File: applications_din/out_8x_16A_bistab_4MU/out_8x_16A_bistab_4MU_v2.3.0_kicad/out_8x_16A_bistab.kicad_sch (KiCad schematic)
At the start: 30 parts, among them IC1 ULN2803A, IC2 ULN2803A, J1 Screw_Terminal_01x02, K1 HFE20-1-024-1HD504, K2 HFE20-1-024-1HD504, K3 HFE20-1-024-1HD504, K4 HFE20-1-024-1HD504, K5 HFE20-1-024-1HD504, K6 HFE20-1-024-1HD504, K7 HFE20-1-024-1HD504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

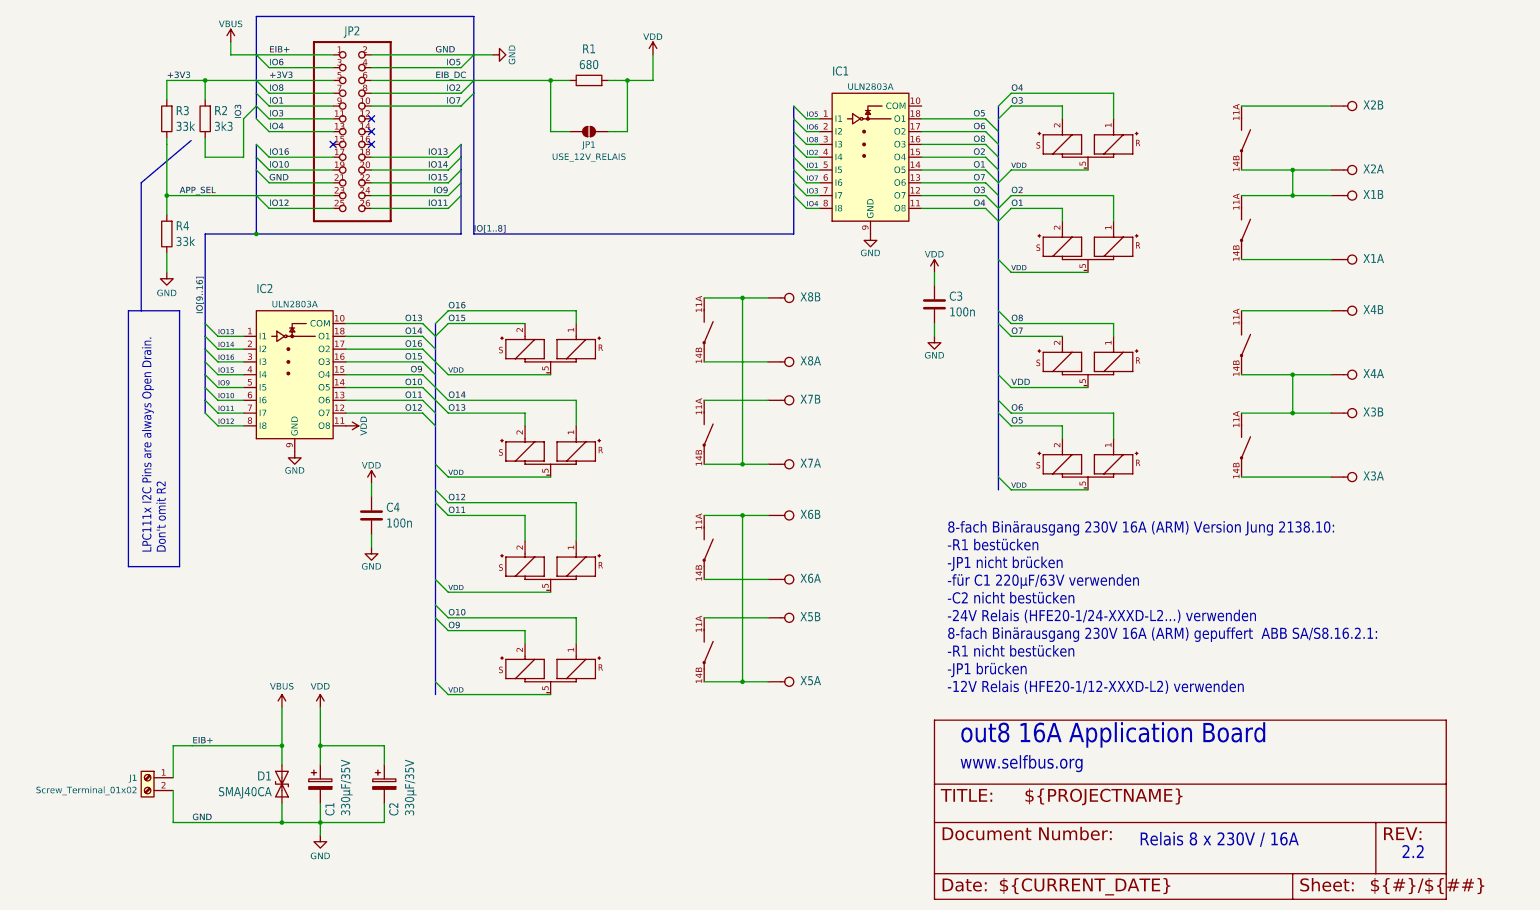
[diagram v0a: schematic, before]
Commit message: out 8x 16A bistab 4MU is now v2.3.0 kicad
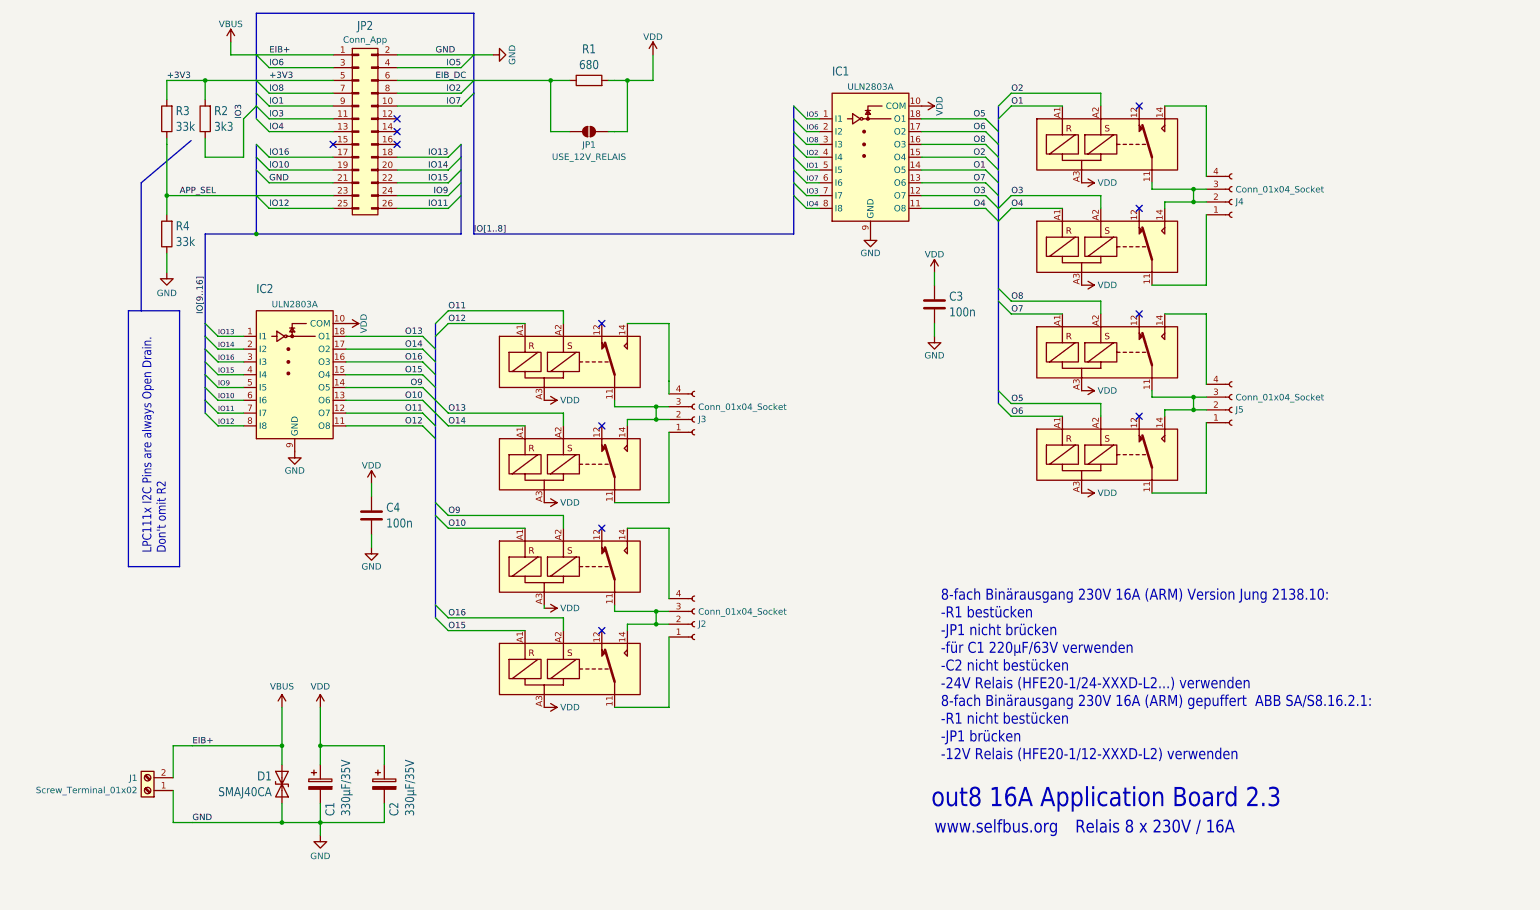
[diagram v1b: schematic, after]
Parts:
- removed unit 2 of K1
- removed unit 2 of K2
- removed unit 2 of K3
- removed unit 2 of K4
- removed unit 2 of K5
- removed unit 2 of K6
- removed unit 2 of K7
- removed unit 2 of K8
- removed X1, X2, X3, X4, X5, X6, X7, X8: W237-02P, out_8x_16A_bistab:W237-132, symbol out_8x_16A_bistab-eagle-import:W237-02P
- added J2, J3, J4, J5: Conn_01x04_Socket, TerminalBlock_Altech:Altech_AK100_1x04_P5.00mm, symbol Connector:Conn_01x04_Socket
- C1, C2: footprint out_8x_16A_bistab:E3,5-8 -> Capacitor_THT:CP_Radial_D8.0mm_P3.50mm
- C3, C4: footprint out_8x_16A_bistab:C1206 -> Capacitor_SMD:C_0805_2012Metric
- IC1, IC2: footprint out_8x_16A_bistab:SO18W -> Package_SO:SOIC-18W_7.5x11.6mm_P1.27mm
- J1: footprint (none) -> selfbus:W243-211_1x02_P5.75
- JP2: value A -> Conn_App; footprint out_8x_16A_bistab:2X13SMD -> Connector_PinHeader_2.54mm:PinHeader_2x13_P2.54mm_Vertical_SMD; symbol out_8x_16A_bistab-eagle-import:PINHD-2X13_2.54-SMD -> Connector_Generic:Conn_02x13_Odd_Even
- K1, K2, K3, K4, K5, K6, K7, K8: footprint out_8x_16A_bistab:HFE20-3-504 -> selfbus:HFE20-1-L2; symbol out_8x_16A_bistab-eagle-import:HFE20-1-024-1HD504 -> selfbus:HFE20-1/24-1HSD-L2
- R1, R2, R3, R4: footprint out_8x_16A_bistab:M1206 -> Resistor_SMD:R_0805_2012Metric
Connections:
- net GND: now also J1.1 (Pin_1); no longer J1.2 (Pin_2)
- net O1: now also K1.A1; no longer K1.2 (S+)
- net O10: now also IC2.13 (O6), K6.A1; no longer IC2.14 (O5), K5.1 (R+)
- net O11: now also IC2.12 (O7), K8.A2; no longer IC2.13 (O6), K6.2 (S+)
- net O12: now also IC2.11 (O8), K8.A1; no longer IC2.12 (O7), K6.1 (R+)
- net O13: now also IC2.18 (O1), K7.A2; no longer IC2.10 (COM), K7.2 (S+)
- net O14: now also IC2.17 (O2), K7.A1; no longer IC2.18 (O1), K7.1 (R+)
- net O15: now also IC2.15 (O4), K5.A1; no longer IC2.16 (O3), K8.2 (S+)
- net O16: now also IC2.16 (O3), K5.A2; no longer IC2.17 (O2), K8.1 (R+)
- net O2: now also K1.A2; no longer K1.1 (R+)
- net O3: now also K2.A2; no longer K2.2 (S+)
- net O4: now also K2.A1; no longer K2.1 (R+)
- net O5: now also K4.A2; no longer K3.2 (S+)
- net O6: now also K4.A1; no longer K3.1 (R+)
- net O7: now also K3.A1; no longer K4.2 (S+)
- net O8: now also K3.A2; no longer K4.1 (R+)
- net O9: now also IC2.14 (O5), K6.A2; no longer IC2.15 (O4), K5.2 (S+)
- net VBUS: now also J1.2 (Pin_2); no longer J1.1 (Pin_1)
- net VDD: now also IC1.10 (COM), IC2.10 (COM), K1.A3, K2.A3, K3.A3, K4.A3, K5.A3, K6.A3, K7.A3, K8.A3; no longer IC2.11 (O8), K1.5 (-), K2.5 (-), K3.5 (-), K4.5 (-), K5.5 (-), K6.5 (-), K7.5 (-), K8.5 (-)
- new net: J2.1 (Pin_1), K5.11
- new net: J2.2 (Pin_2), J2.3 (Pin_3), K5.14, K6.11
- new net: J2.4 (Pin_4), K6.14
- new net: J3.1 (Pin_1), K7.11
- new net: J3.2 (Pin_2), J3.3 (Pin_3), K7.14, K8.11
- new net: J3.4 (Pin_4), K8.14
- new net: J5.2 (Pin_2), J5.3 (Pin_3), K3.11, K4.14
- new net: J5.4 (Pin_4), K3.14
- new net: J4.2 (Pin_2), J4.3 (Pin_3), K1.11, K2.14
- new net: J4.4 (Pin_4), K1.14
- new net: J4.1 (Pin_1), K2.11
- new net: J5.1 (Pin_1), K4.11
- no-connect marks 4 -> 12
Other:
- note added: "out8 16A Application Board 2.3"
- note removed: "2.2"
- note removed: "out8 16A Application Board"
- moved on the sheet: J1

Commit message: update out_8x_16A_bistab_4MU_v2.3.0_kicad - final for now
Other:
- moved on the sheet: JP1, R1
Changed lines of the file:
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@@
 	)
 	(junction
-		(at 119.38 35.56)
+		(at 113.03 35.56)
 		(diameter 0)
 		(color 0 0 0 0)
@@
 	)
 	(junction
-		(at 104.14 35.56)
+		(at 97.79 35.56)
 		(diameter 0)
 		(color 0 0 0 0)
@@
 	(wire
 		(pts
-			(xy 115.57 35.56) (xy 116.84 35.56)
+			(xy 109.22 35.56) (xy 110.49 35.56)
 		)
 		(stroke
@@
 	(wire
 		(pts
-			(xy 116.84 35.56) (xy 119.38 35.56)
+			(xy 110.49 35.56) (xy 113.03 35.56)
 		)
 		(stroke
@@
 	(wire
 		(pts
-			(xy 119.38 35.56) (xy 124.46 35.56)
+			(xy 113.03 35.56) (xy 118.11 35.56)
 		)
 		(stroke
@@
 	(wire
 		(pts
-			(xy 124.46 35.56) (xy 124.46 30.48)
+			(xy 118.11 35.56) (xy 118.11 30.48)
 		)
 		(stroke
@@
 	(wire
 		(pts
-			(xy 119.38 45.72) (xy 116.84 45.72)
+			(xy 113.03 45.72) (xy 110.49 45.72)
 		)
 		(stroke
@@
 	(wire
 		(pts
-			(xy 115.57 45.72) (xy 116.84 45.72)
+			(xy 109.22 45.72) (xy 110.49 45.72)
 		)
 		(stroke
@@
 	(wire
 		(pts
-			(xy 88.9 35.56) (xy 104.14 35.56)
+			(xy 88.9 35.56) (xy 97.79 35.56)
 		)
 		(stroke
@@
 	(wire
 		(pts
-			(xy 104.14 45.72) (xy 107.95 45.72)
+			(xy 97.79 45.72) (xy 101.6 45.72)
 		)
 		(stroke
@@
 	(wire
 		(pts
-			(xy 104.14 35.56) (xy 107.95 35.56)
+			(xy 97.79 35.56) (xy 101.6 35.56)
 		)
 		(stroke
@@
 	(wire
 		(pts
-			(xy 104.14 35.56) (xy 104.14 45.72)
+			(xy 97.79 35.56) (xy 97.79 45.72)
 		)
 		(stroke
@@
 	(wire
 		(pts
-			(xy 119.38 35.56) (xy 119.38 45.72)
+			(xy 113.03 35.56) (xy 113.03 45.72)
 		)
 		(stroke
@@
 	(symbol
 		(lib_id "Device:R")
-		(at 111.76 35.56 90)
+		(at 105.41 35.56 90)
 		(unit 1)
 		(exclude_from_sim no)
@@
 		(fields_autoplaced yes)
 		(property "Reference" "R1"
-			(at 111.76 29.3494 90)
+			(at 105.41 29.3494 90)
 			(effects
 				(font
@@
 		)
 		(property "Value" "680"
-			(at 111.76 32.4738 90)
+			(at 105.41 32.4738 90)
 			(effects
 				(font
@@
 		)
 		(property "Footprint" "Resistor_SMD:R_0805_2012Metric"
-			(at 111.76 37.338 90)
+			(at 105.41 37.338 90)
 			(effects
 				(font
@@
 		)
 		(property "Datasheet" "~"
-			(at 111.76 35.56 0)
+			(at 105.41 35.56 0)
 			(effects
 				(font
@@
 		)
 		(property "Description" "Resistor"
-			(at 111.76 35.56 0)
+			(at 105.41 35.56 0)
 			(effects
 				(font
@@
 	(symbol
 		(lib_id "power:VDD")
-		(at 124.46 30.48 0)
+		(at 118.11 30.48 0)
 		(unit 1)
 		(exclude_from_sim no)
@@
 		(dnp no)
 		(property "Reference" "#PWR0104"
-			(at 124.46 34.29 0)
+			(at 118.11 34.29 0)
 			(effects
 				(font
@@
 		)
 		(property "Value" "VDD"
-			(at 124.46 26.924 0)
+			(at 118.11 26.924 0)
 			(effects
 				(font
@@
 		)
 		(property "Footprint" ""
-			(at 124.46 30.48 0)
+			(at 118.11 30.48 0)
 			(effects
 				(font
@@
 		)
 		(property "Datasheet" ""
-			(at 124.46 30.48 0)
+			(at 118.11 30.48 0)
 			(effects
 				(font
@@
 		)
 		(property "Description" "Power symbol creates a global label with name \"VDD\""
-			(at 124.46 30.48 0)
+			(at 118.11 30.48 0)
 			(effects
 				(font
@@
 	(symbol
 		(lib_id "Jumper:SolderJumper_2_Open")
-		(at 111.76 45.72 0)
+		(at 105.41 45.72 0)
 		(unit 1)
 		(exclude_from_sim yes)
@@
 		(fields_autoplaced yes)
 		(property "Reference" "JP1"
-			(at 111.76 48.3291 0)
+			(at 105.41 48.3291 0)
 			(effects
 				(font
@@
 		)
 		(property "Value" "USE_12V_RELAIS"
-			(at 111.76 50.7534 0)
+			(at 105.41 50.7534 0)
 			(effects
 				(font
@@
 		)
 		(property "Footprint" "Jumper:SolderJumper-2_P1.3mm_Open_Pad1.0x1.5mm"
-			(at 111.76 45.72 0)
+			(at 105.41 45.72 0)
 			(effects
 				(font
@@
 		)
 		(property "Datasheet" "~"
-			(at 111.76 45.72 0)
+			(at 105.41 45.72 0)
 			(effects
 				(font
@@
 		)
 		(property "Description" "Solder Jumper, 2-pole, open"
-			(at 111.76 45.72 0)
+			(at 105.41 45.72 0)
 			(effects
 				(font

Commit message: update all stuff
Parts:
- J1: value Screw_Terminal_01x02 -> EIB_WAGO_243-211
- J6: renamed from JP2; footprint Connector_PinHeader_2.54mm:PinHeader_2x13_P2.54mm_Vertical_SMD -> Connector_IDC:IDC-Header_2x13_P2.54mm_Vertical_SMD
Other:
- moved on the sheet: J2, J3, J4, J5

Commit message: finally standardize selected parts on all boards
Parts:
- added D2: 12V, Diode_SMD:D_MiniMELF, symbol Device:D_Zener
- J2, J3, J4, J5: value Conn_01x04_Socket -> Con_230V
- R1: footprint Resistor_SMD:R_0805_2012Metric -> Resistor_SMD:R_1206_3216Metric
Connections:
- net GND: now also D2.2 (A)
- net VDD: now also D2.1 (K)
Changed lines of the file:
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@@
 	(wire
 		(pts
+			(xy 118.11 44.45) (xy 118.11 45.72)
+		)
+		(stroke
+			(width 0)
+			(type default)
+		)
+	)
+	(wire
+		(pts
 			(xy 97.79 35.56) (xy 97.79 45.72)
 		)
@@
 	(wire
 		(pts
+			(xy 118.11 35.56) (xy 118.11 36.83)
+		)
+		(stroke
+			(width 0)
+			(type default)
+		)
+	)
+	(wire
+		(pts
 			(xy 226.06 101.6) (xy 226.06 102.87)
 		)
@@
 		(on_board yes)
 		(dnp no)
+		(fields_autoplaced yes)
 		(property "Reference" "J2"
-			(at 134.0612 143.4522 0)
+			(at 132.715 133.8283 0)
 			(effects
 				(font
 					(size 1.27 1.27)
 				)
-				(justify left)
 			)
 		)
-		(property "Value" "Conn_01x04_Socket"
-			(at 134.0612 141.0279 0)
+		(property "Value" "Con_230V"
+			(at 132.715 136.2526 0)
 			(effects
 				(font
 					(size 1.27 1.27)
 				)
-				(justify left)
 			)
 		)
@@
 			)
 		)
-		(property "Footprint" "Resistor_SMD:R_0805_2012Metric"
+		(property "Footprint" "Resistor_SMD:R_1206_3216Metric"
 			(at 105.41 37.338 90)
 			(effects
@@
 	)
 	(symbol
+		(lib_id "Device:D_Zener")
+		(at 118.11 40.64 270)
+		(unit 1)
+		(exclude_from_sim no)
+		(in_bom yes)
+		(on_board yes)
+		(dnp no)
+		(fields_autoplaced yes)
+		(property "Reference" "D2"
+			(at 120.142 39.4278 90)
+			(effects
+				(font
+					(size 1.27 1.27)
+				)
+				(justify left)
+			)
+		)
+		(property "Value" "12V"
+			(at 120.142 41.8521 90)
+			(effects
+				(font
+					(size 1.27 1.27)
+				)
+				(justify left)
+			)
+		)
+		(property "Footprint" "Diode_SMD:D_MiniMELF"
+			(at 118.11 40.64 0)
+			(effects
+				(font
+					(size 1.27 1.27)
+				)
+				(hide yes)
+			)
+		)
+		(property "Datasheet" "~"
+			(at 118.11 40.64 0)
+			(effects
+				(font
+					(size 1.27 1.27)
+				)
+				(hide yes)
+			)
+		)
+		(property "Description" "Zener diode"
+			(at 118.11 40.64 0)
+			(effects
+				(font
+					(size 1.27 1.27)
+				)
+				(hide yes)
+			)
+		)
+		(pin "2"
+		)
+		(pin "1"
+		)
+		(instances
+			(project ""
+				(path "/e17a8f7c-290a-48c4-8119-0faa75a2ce74"
+					(reference "D2")
+					(unit 1)
+				)
+			)
+		)
+	)
+	(symbol
 		(lib_id "Transistor_Array:ULN2803A")
 		(at 167.64 48.26 0)
@@
 	)
 	(symbol
+		(lib_id "power:GND")
+		(at 118.11 45.72 0)
+		(unit 1)
+		(exclude_from_sim no)
+		(in_bom yes)
+		(on_board yes)
+		(dnp no)
+		(property "Reference" "#PWR018"
+			(at 118.11 52.07 0)
+			(effects
+				(font
+					(size 1.27 1.27)
+				)
+				(hide yes)
+			)
+		)
+		(property "Value" "GND"
+			(at 118.11 49.53 0)
+			(effects
+				(font
+					(size 1.27 1.27)
+				)
+			)
+		)
+		(property "Footprint" ""
+			(at 118.11 45.72 0)
+			(effects
+				(font
+					(size 1.27 1.27)
+				)
+				(hide yes)
+			)
+		)
+		(property "Datasheet" ""
+			(at 118.11 45.72 0)
+			(effects
+				(font
+					(size 1.27 1.27)
+				)
+				(hide yes)
+			)
+		)
+		(property "Description" "Power symbol creates a global label with name \"GND\" , ground"
+			(at 118.11 45.72 0)
+			(effects
+				(font
+					(size 1.27 1.27)
+				)
+				(hide yes)
+			)
+		)
+		(pin "1"
+		)
+		(instances
+			(project "out_8x_16A_bistab"
+				(path "/e17a8f7c-290a-48c4-8119-0faa75a2ce74"
+					(reference "#PWR018")
+					(unit 1)
+				)
+			)
+		)
+	)
+	(symbol
 		(lib_id "power:PWR_FLAG")
 		(at 39.37 167.64 0)
@@
 		(on_board yes)
 		(dnp no)
+		(fields_autoplaced yes)
 		(property "Reference" "J4"
-			(at 240.7412 59.6322 0)
+			(at 239.395 50.0083 0)
 			(effects
 				(font
 					(size 1.27 1.27)
 				)
-				(justify left)
 			)
 		)
-		(property "Value" "Conn_01x04_Socket"
-			(at 240.7412 57.2079 0)
+		(property "Value" "Con_230V"
+			(at 239.395 52.4326 0)
 			(effects
 				(font
 					(size 1.27 1.27)
 				)
-				(justify left)
 			)
 		)
@@
 		(on_board yes)
 		(dnp no)
+		(fields_autoplaced yes)
 		(property "Reference" "J5"
-			(at 240.7412 101.5422 0)
+			(at 239.395 91.9183 0)
 			(effects
 				(font
 					(size 1.27 1.27)
 				)
-				(justify left)
 			)
 		)
-		(property "Value" "Conn_01x04_Socket"
-			(at 240.7412 99.1179 0)
+		(property "Value" "Con_230V"
+			(at 239.395 94.3426 0)
 			(effects
 				(font
 					(size 1.27 1.27)
 				)
-				(justify left)
 			)
 		)
@@
 		(on_board yes)
 		(dnp no)
+		(fields_autoplaced yes)
 		(property "Reference" "J3"
-			(at 134.0612 102.8122 0)
+			(at 132.715 93.1883 0)
 			(effects
 				(font
 					(size 1.27 1.27)
 				)
-				(justify left)
 			)
 		)
-		(property "Value" "Conn_01x04_Socket"
-			(at 134.0612 100.3879 0)
+		(property "Value" "Con_230V"
+			(at 132.715 95.6126 0)
 			(effects
 				(font
 					(size 1.27 1.27)
 				)
-				(justify left)
 			)
 		)

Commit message: final for manufacturing
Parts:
- J1: value EIB_WAGO_243-211 -> WAGO-243-211
- K1, K2, K3, K4, K5, K6, K7, K8: value HFE20-1-024-1HD504 -> HFE20-1/24-1HSD-L2
- R1: value 680 -> 680 500mW
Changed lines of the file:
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@@
 			)
 		)
-		(property "Value" "680"
+		(property "Value" "680 500mW"
 			(at 105.41 32.4738 90)
 			(effects
@@
 		(on_board yes)
 		(dnp no)
+		(fields_autoplaced yes)
 		(property "Reference" "K7"
-			(at 111.76 111.125 0)
+			(at 122.682 110.1978 0)
 			(effects
 				(font
 					(size 1.778 1.5113)
 				)
-				(justify left bottom)
-				(hide yes)
+				(justify left)
 			)
 		)
-		(property "Value" "HFE20-1-024-1HD504"
-			(at 110.49 108.204 0)
+		(property "Value" "HFE20-1/24-1HSD-L2"
+			(at 122.682 113.3222 0)
 			(effects
 				(font
 					(size 1.778 1.5113)
 				)
-				(justify left bottom)
-				(hide yes)
+				(justify left)
 			)
 		)
@@
 		(on_board yes)
 		(dnp no)
+		(fields_autoplaced yes)
 		(property "Reference" "K8"
-			(at 111.76 90.805 0)
+			(at 122.682 89.8778 0)
 			(effects
 				(font
 					(size 1.778 1.5113)
 				)
-				(justify left bottom)
-				(hide yes)
+				(justify left)
 			)
 		)
-		(property "Value" "HFE20-1-024-1HD504"
-			(at 110.49 87.884 0)
+		(property "Value" "HFE20-1/24-1HSD-L2"
+			(at 122.682 93.0022 0)
 			(effects
 				(font
 					(size 1.778 1.5113)
 				)
-				(justify left bottom)
-				(hide yes)
+				(justify left)
 			)
 		)
@@
 		(on_board yes)
 		(dnp no)
+		(fields_autoplaced yes)
 		(property "Reference" "K6"
-			(at 111.76 131.445 0)
+			(at 122.682 130.5178 0)
 			(effects
 				(font
 					(size 1.778 1.5113)
 				)
-				(justify left bottom)
-				(hide yes)
+				(justify left)
 			)
 		)
-		(property "Value" "HFE20-1-024-1HD504"
-			(at 110.49 128.524 0)
+		(property "Value" "HFE20-1/24-1HSD-L2"
+			(at 122.682 133.6422 0)
 			(effects
 				(font
 					(size 1.778 1.5113)
 				)
-				(justify left bottom)
-				(hide yes)
+				(justify left)
 			)
 		)
@@
 		(on_board yes)
 		(dnp no)
+		(fields_autoplaced yes)
 		(property "Reference" "K3"
-			(at 218.44 89.535 0)
+			(at 229.362 88.6078 0)
 			(effects
 				(font
 					(size 1.778 1.5113)
 				)
-				(justify left bottom)
-				(hide yes)
+				(justify left)
 			)
 		)
-		(property "Value" "HFE20-1-024-1HD504"
-			(at 217.17 86.614 0)
+		(property "Value" "HFE20-1/24-1HSD-L2"
+			(at 229.362 91.7322 0)
 			(effects
 				(font
 					(size 1.778 1.5113)
 				)
-				(justify left bottom)
-				(hide yes)
+				(justify left)
 			)
 		)
@@
 		(on_board yes)
 		(dnp no)
+		(fields_autoplaced yes)
 		(property "Reference" "K1"
-			(at 218.44 47.625 0)
+			(at 229.362 46.6978 0)
 			(effects
 				(font
 					(size 1.778 1.5113)
 				)
-				(justify left bottom)
-				(hide yes)
+				(justify left)
 			)
 		)
-		(property "Value" "HFE20-1-024-1HD504"
-			(at 217.17 44.704 0)
+		(property "Value" "HFE20-1/24-1HSD-L2"
+			(at 229.362 49.8222 0)
 			(effects
 				(font
 					(size 1.778 1.5113)
 				)
-				(justify left bottom)
-				(hide yes)
+				(justify left)
 			)
 		)
@@
 			)
 		)
-		(property "Value" "EIB_WAGO_243-211"
+		(property "Value" "WAGO-243-211"
 			(at 22.0981 176.4721 0)
 			(effects
@@
 		(on_board yes)
 		(dnp no)
+		(fields_autoplaced yes)
 		(property "Reference" "K4"
-			(at 218.44 109.855 0)
+			(at 199.898 108.9278 0)
 			(effects
 				(font
 					(size 1.778 1.5113)
 				)
-				(justify left bottom)
-				(hide yes)
+				(justify right)
 			)
 		)
-		(property "Value" "HFE20-1-024-1HD504"
-			(at 217.17 106.934 0)
+		(property "Value" "HFE20-1/24-1HSD-L2"
+			(at 199.898 112.0522 0)
 			(effects
 				(font
 					(size 1.778 1.5113)
 				)
-				(justify left bottom)
-				(hide yes)
+				(justify right)
 			)
 		)
@@
 		(on_board yes)
 		(dnp no)
+		(fields_autoplaced yes)
 		(property "Reference" "K2"
-			(at 218.44 67.945 0)
+			(at 229.362 67.0178 0)
 			(effects
 				(font
 					(size 1.778 1.5113)
 				)
-				(justify left bottom)
-				(hide yes)
+				(justify left)
 			)
 		)
-		(property "Value" "HFE20-1-024-1HD504"
-			(at 217.17 65.024 0)
+		(property "Value" "HFE20-1/24-1HSD-L2"
+			(at 229.362 70.1422 0)
 			(effects
 				(font
 					(size 1.778 1.5113)
 				)
-				(justify left bottom)
-				(hide yes)
+				(justify left)
 			)
 		)
@@
 		(on_board yes)
 		(dnp no)
+		(fields_autoplaced yes)
 		(property "Reference" "K5"
-			(at 111.76 151.765 0)
+			(at 93.218 150.8378 0)
 			(effects
 				(font
 					(size 1.778 1.5113)
 				)
-				(justify left bottom)
-				(hide yes)
+				(justify right)
 			)
 		)
-		(property "Value" "HFE20-1-024-1HD504"
-			(at 110.49 148.844 0)
+		(property "Value" "HFE20-1/24-1HSD-L2"
+			(at 93.218 153.9622 0)
 			(effects
 				(font
 					(size 1.778 1.5113)
 				)
-				(justify left bottom)
-				(hide yes)
+				(justify right)
 			)
 		)
